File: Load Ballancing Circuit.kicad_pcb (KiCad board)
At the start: 2 copper layers, 33 x 38.3 mm, 30 parts, among them J2 171857-0005, J3 171857-0004, J4 171857-0006, U1 LTC4359HMS8#PBF, U2 LTC4359HMS8#PBF, U3 INA139, U4 MAX11615, U5 INA139

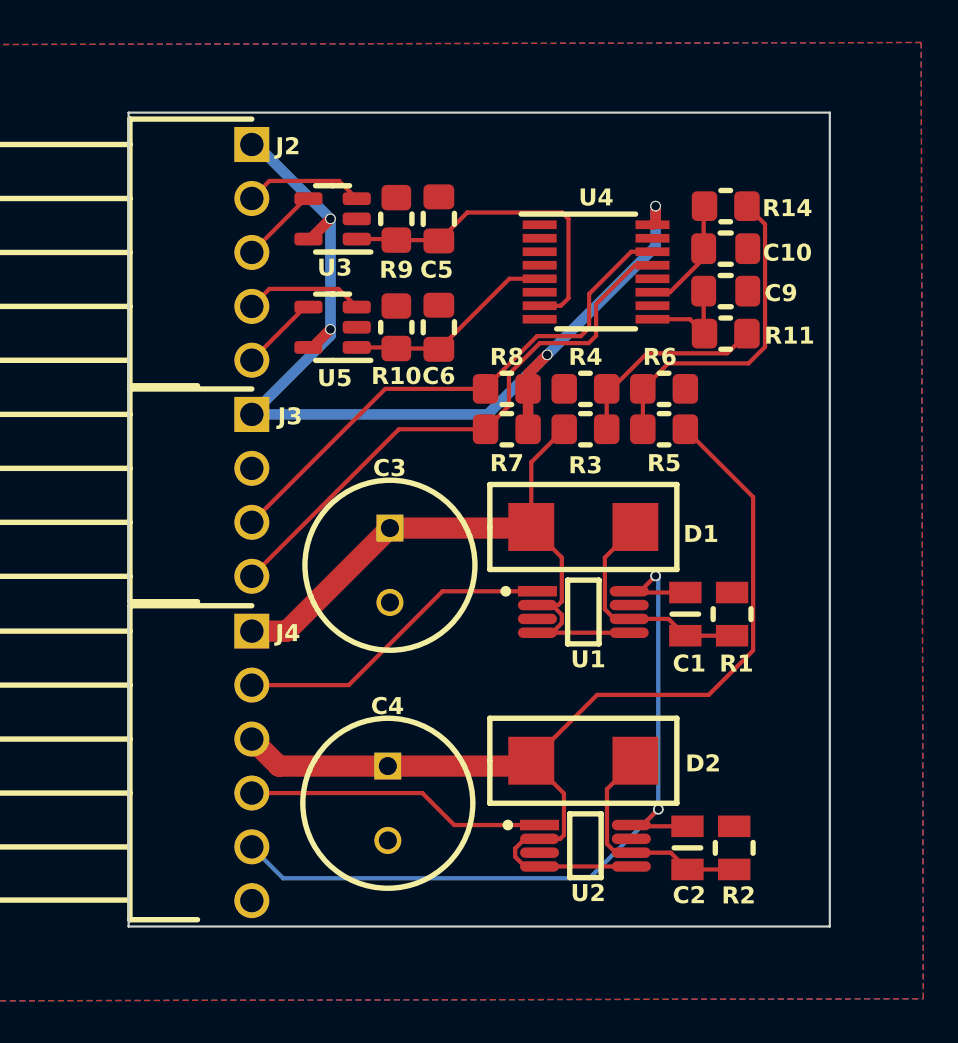
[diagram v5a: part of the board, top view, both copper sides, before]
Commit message: fixed drc issues
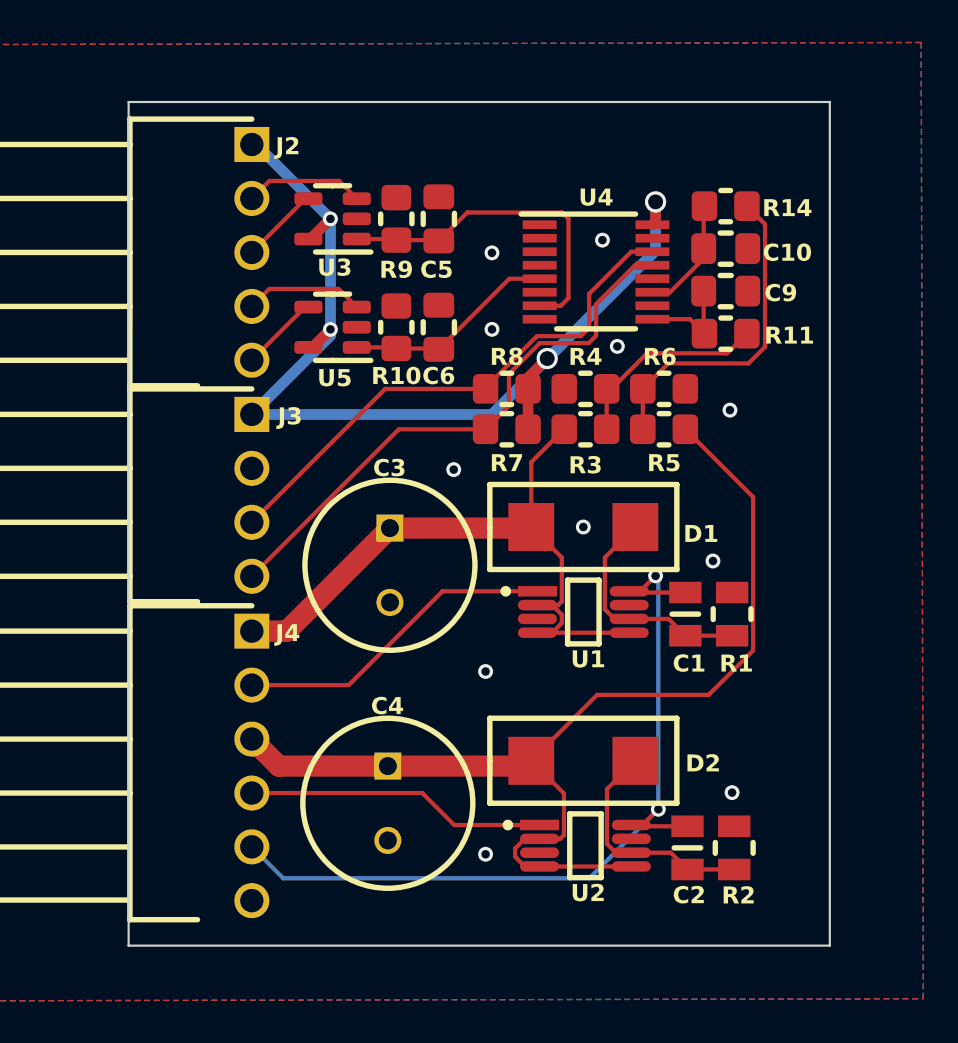
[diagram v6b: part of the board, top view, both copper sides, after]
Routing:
- net GND: vias 0 -> 11
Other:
- board size 33 x 38.3 mm -> 33 x 39.7 mm
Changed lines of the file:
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@@
     )
   )
-  (gr_rect (start 149.8511 71.7331) (end 182.8511 110.0331)
+  (gr_rect (start 149.8511 71.2331) (end 182.8511 110.9331)
     (stroke (width 0.1016) (type default)) (fill none) (layer "Edge.Cuts"))
   (dimension (type aligned) (layer "Dwgs.User")
@@
   (segment (start 173.46995 94.3171) (end 176.0511 94.3171) (width 0.2) (layer "F.Cu") (net 1))
   (segment (start 173.41095 94.2581) (end 173.46995 94.3171) (width 0.2) (layer "F.Cu") (net 1))
-  (via (at 174.780602 104.517081) (size 0.508) (drill 0.35) (layers "F.Cu" "B.Cu") (net 1))
-  (via (at 174.6511 93.5331) (size 0.508) (drill 0.35) (layers "F.Cu" "B.Cu") (net 1))
+  (via (at 174.780602 104.517081) (size 0.7) (drill 0.4) (layers "F.Cu" "B.Cu") (net 1))
+  (via (at 174.6511 93.5331) (size 0.7) (drill 0.4) (layers "F.Cu" "B.Cu") (net 1))
   (segment (start 174.780602 93.662602) (end 174.780602 104.517081) (width 0.2) (layer "B.Cu") (net 1))
   (segment (start 174.6511 93.5331) (end 174.780602 93.662602) (width 0.2) (layer "B.Cu") (net 1))
@@
   (segment (start 170.162925 105.9081) (end 170.33846 105.732565) (width 0.2) (layer "F.Cu") (net 5))
   (segment (start 168.5511 102.4831) (end 168.8011 102.2331) (width 1) (layer "F.Cu") (net 5))
+  (via (at 166.6511 106.6331) (size 0.7) (drill 0.4) (layers "F.Cu" "B.Cu") (free) (net 6))
+  (via (at 172.8511 82.7331) (size 0.7) (drill 0.4) (layers "F.Cu" "B.Cu") (free) (net 6))
+  (via (at 171.2511 91.2331) (size 0.7) (drill 0.4) (layers "F.Cu" "B.Cu") (free) (net 6))
+  (via (at 165.1511 88.5331) (size 0.7) (drill 0.4) (layers "F.Cu" "B.Cu") (free) (net 6))
+  (via (at 166.9511 81.9331) (size 0.7) (drill 0.4) (layers "F.Cu" "B.Cu") (free) (net 6))
+  (via (at 178.1511 85.7331) (size 0.7) (drill 0.4) (layers "F.Cu" "B.Cu") (free) (net 6))
+  (via (at 172.1511 77.7331) (size 0.7) (drill 0.4) (layers "F.Cu" "B.Cu") (free) (net 6))
+  (via (at 166.6511 98.0331) (size 0.7) (drill 0.4) (layers "F.Cu" "B.Cu") (free) (net 6))
+  (via (at 177.3511 92.8331) (size 0.7) (drill 0.4) (layers "F.Cu" "B.Cu") (free) (net 6))
+  (via (at 178.2511 103.7331) (size 0.7) (drill 0.4) (layers "F.Cu" "B.Cu") (free) (net 6))
+  (via (at 166.9511 78.3331) (size 0.7) (drill 0.4) (layers "F.Cu" "B.Cu") (free) (net 6))
   (segment (start 160.2111 98.6731) (end 155.6511 98.6731) (width 0.2) (layer "F.Cu") (net 7))
   (segment (start 169.09125 94.2581) (end 164.6261 94.2581) (width 0.2) (layer "F.Cu") (net 7))
@@
   (segment (start 158.4011 77.6831) (end 159.3511 76.7331) (width 0.5) (layer "F.Cu") (net 15))
   (segment (start 168.6511 84.7331) (end 168.6511 86.6331) (width 0.5) (layer "F.Cu") (net 15))
+  (segment (start 174.6511 75.9331) (end 174.6511 76.8649) (width 0.5) (layer "F.Cu") (net 15))
   (segment (start 158.3136 77.6831) (end 158.4011 77.6831) (width 0.5) (layer "F.Cu") (net 15))
-  (segment (start 168.6511 84.7331) (end 168.6511 84.0331) (width 0.5) (layer "F.Cu") (net 15))
+  (segment (start 168.6511 84.2056) (end 168.6511 84.7331) (width 0.5) (layer "F.Cu") (net 15))
   (segment (start 174.6511 76.8649) (end 174.5054 77.0106) (width 0.5) (layer "F.Cu") (net 15))
+  (segment (start 169.5511 83.3056) (end 168.6511 84.2056) (width 0.5) (layer "F.Cu") (net 15))
   (segment (start 158.5011 82.7831) (end 159.3511 81.9331) (width 0.5) (layer "F.Cu") (net 15))
-  (segment (start 174.6511 76.1331) (end 174.6511 76.8649) (width 0.5) (layer "F.Cu") (net 15))
-  (segment (start 168.6511 84.0331) (end 169.5511 83.1331) (width 0.5) (layer "F.Cu") (net 15))
-  (via (at 159.3511 76.7331) (size 0.5) (drill 0.4) (layers "F.Cu" "B.Cu") (net 15))
-  (via (at 174.6511 76.1331) (size 0.5) (drill 0.4) (layers "F.Cu" "B.Cu") (net 15))
-  (via (at 159.3511 81.9331) (size 0.5) (drill 0.4) (layers "F.Cu" "B.Cu") (net 15))
-  (via (at 169.5511 83.1331) (size 0.5) (drill 0.4) (layers "F.Cu" "B.Cu") (net 15))
+  (via (at 159.3511 76.7331) (size 0.7) (drill 0.4) (layers "F.Cu" "B.Cu") (net 15))
+  (via (at 174.6511 75.9331) (size 1) (drill 0.7) (layers "F.Cu" "B.Cu") (net 15))
+  (via (at 159.3511 81.9331) (size 0.7) (drill 0.4) (layers "F.Cu" "B.Cu") (net 15))
+  (via (at 169.5511 83.3056) (size 1) (drill 0.7) (layers "F.Cu" "B.Cu") (net 15))
   (segment (start 159.3511 82.2331) (end 159.3511 81.9331) (width 0.5) (layer "B.Cu") (net 15))
   (segment (start 159.3511 81.9331) (end 159.3511 76.7331) (width 0.5) (layer "B.Cu") (net 15))
+  (segment (start 174.6511 78.2331) (end 169.5786 83.3056) (width 0.5) (layer "B.Cu") (net 15))
+  (segment (start 169.5511 83.3056) (end 169.5511 83.3331) (width 0.5) (layer "B.Cu") (net 15))
+  (segment (start 166.9511 85.9331) (end 155.6511 85.9331) (width 0.5) (layer "B.Cu") (net 15))
+  (segment (start 169.5786 83.3056) (end 169.5511 83.3056) (width 0.5) (layer "B.Cu") (net 15))
+  (segment (start 169.5511 83.3331) (end 166.9511 85.9331) (width 0.5) (layer "B.Cu") (net 15))
   (segment (start 159.3511 76.7331) (end 155.8511 73.2331) (width 0.5) (layer "B.Cu") (net 15))
-  (segment (start 174.6511 78.0331) (end 174.6511 76.1331) (width 0.5) (layer "B.Cu") (net 15))
-  (segment (start 169.5511 83.1331) (end 166.7511 85.9331) (width 0.5) (layer "B.Cu") (net 15))
+  (segment (start 174.6511 75.9331) (end 174.6511 78.2331) (width 0.5) (layer "B.Cu") (net 15))
   (segment (start 155.6511 85.9331) (end 159.3511 82.2331) (width 0.5) (layer "B.Cu") (net 15))
-  (segment (start 166.7511 85.9331) (end 155.6511 85.9331) (width 0.5) (layer "B.Cu") (net 15))
-  (segment (start 169.5511 83.1331) (end 174.6511 78.0331) (width 0.5) (layer "B.Cu") (net 15))
   (segment (start 155.8511 73.2331) (end 155.6511 73.2331) (width 0.5) (layer "B.Cu") (net 15))
   (segment (start 174.5054 78.2806) (end 173.5054 78.2806) (width 0.2) (layer "F.Cu") (net 16))
@@
   (segment (start 175.2511 83.5331) (end 174.0511 84.7331) (width 0.2) (layer "F.Cu") (net 29))
   (zone (net 6) (net_name "GND") (layers "F&B.Cu") (hatch edge 0.5)
-    (connect_pads yes (clearance 0.25))
-    (min_thickness 0.25) (filled_areas_thickness no)
-    (fill yes (thermal_gap 0.5) (thermal_bridge_width 0.5))
+    (connect_pads thru_hole_only (clearance 0.1))
+    (min_thickness 0.1) (filled_areas_thickness no)
+    (fill yes (thermal_gap 0.5) (thermal_bridge_width 0.5) (island_removal_mode 2) (island_area_min 10))
     (polygon
       (pts
